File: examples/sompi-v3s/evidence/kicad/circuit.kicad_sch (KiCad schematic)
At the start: 132 parts, among them J1 USB-C 16P, J2 RJ45 HR911105A, J3 microSD, J4 LCD 40P RGB, J5 CAM MIPI 24P, J6 3.5mm jack, J7 GPIO 2x13, J8 UART0 debug, Q1 AO3400A, SW1 RESET, SW2 KEY1, U1 Allwinner V3s, U2 TPS562200, U3 TPS562200, U4 ME6211C18M5G, U5 XC6206P302MR, U6 W25Q128JVSIQ, U8 USBLC6-2SC6, Y1 24MHz, Y2 32.768kHz

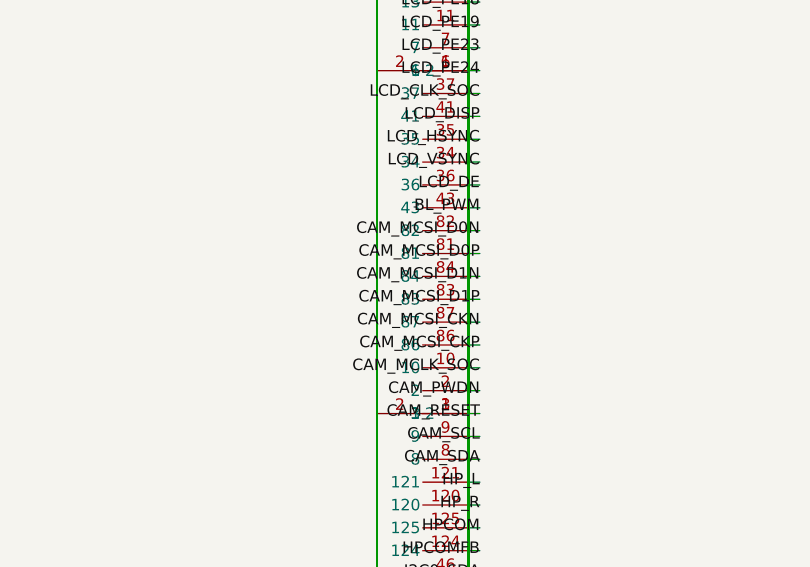
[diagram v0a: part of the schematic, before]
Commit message: evidence: SomPi-V3s rebuilt with someda 0.7.0 — 7 of 7 pairs coupled within skew budget, 0 crosstalk violations, kicad-cli DRC 0 errors, 6/6 gates
Co-Authored-By: Claude Fable 5.1 <noreply@anthropic.com>
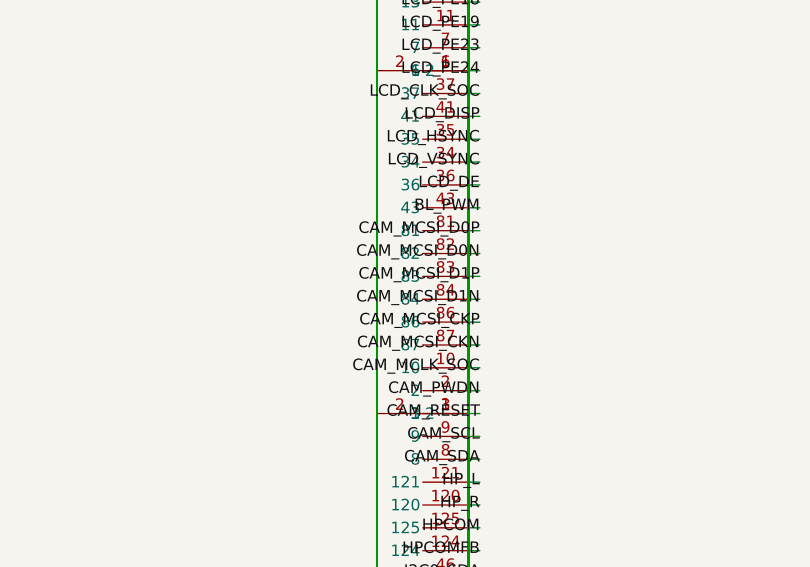
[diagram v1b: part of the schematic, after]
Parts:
- U1: symbol SoC:Allwinner_V3s__p129_12_29_50_57_104_127_85_93_98_109_122_19_58_64_80_108_126_20_21_25_26_38_47_51_56_88_59_60_61_62_65_66_67_68_69_70_72_79_76_115_97_116_123_71_63_73_117_118_94_75_74_96_95_99_112_42_111_110_92_91_90_89_77_78_101_102_103_106_107_105_100_54_52_55_53_33_32_31_30_28_27_24_23_22_18_17_16_15_14_13_11_7_6_37_41_35_34_36_43_82_81_84_83_87_86_10_2_3_9_8_121_120_125_124_46_45_5_39_40_4_44_1_128_48_49 -> SoC:Allwinner_V3s__p129_12_29_50_57_104_127_85_93_98_109_122_19_58_64_80_108_126_20_21_25_26_38_47_51_56_88_59_60_61_62_65_66_67_68_69_70_72_79_76_115_97_116_123_71_63_73_117_118_94_75_74_96_95_99_112_42_111_110_92_91_90_89_77_78_101_102_103_106_107_105_100_54_52_55_53_33_32_31_30_28_27_24_23_22_18_17_16_15_14_13_11_7_6_37_41_35_34_36_43_81_82_83_84_86_87_10_2_3_9_8_121_120_125_124_46_45_5_39_40_4_44_1_128_48_49
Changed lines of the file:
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@@
   (wire (pts (xy 45.72 2141.22) (xy 45.72 2222.50)) (uuid wire_1144) )
   (wire (pts (xy 55.88 144.78) (xy 57.15 144.78)) (uuid wire_1145) )
-  (label "CAM_MCSI_D0N" (at 57.15 144.78 180))
+  (label "CAM_MCSI_D0P" (at 57.15 144.78 180))
   (wire (pts (xy 55.88 147.32) (xy 55.88 2136.14)) (uuid wire_1146) )
   (wire (pts (xy 55.88 2136.14) (xy 55.88 2136.14)) (uuid wire_1147) )
   (wire (pts (xy 55.88 2136.14) (xy 55.88 2222.50)) (uuid wire_1148) )
   (wire (pts (xy 55.88 147.32) (xy 57.15 147.32)) (uuid wire_1149) )
-  (label "CAM_MCSI_D0P" (at 57.15 147.32 180))
+  (label "CAM_MCSI_D0N" (at 57.15 147.32 180))
   (wire (pts (xy 55.88 149.86) (xy 55.88 2131.06)) (uuid wire_1150) )
   (wire (pts (xy 55.88 2131.06) (xy 55.88 2131.06)) (uuid wire_1151) )
   (wire (pts (xy 55.88 2131.06) (xy 55.88 2225.04)) (uuid wire_1152) )
   (wire (pts (xy 55.88 149.86) (xy 57.15 149.86)) (uuid wire_1153) )
-  (label "CAM_MCSI_D1N" (at 57.15 149.86 180))
+  (label "CAM_MCSI_D1P" (at 57.15 149.86 180))
   (wire (pts (xy 55.88 152.40) (xy 55.88 2125.98)) (uuid wire_1154) )
   (wire (pts (xy 55.88 2125.98) (xy 55.88 2125.98)) (uuid wire_1155) )
   (wire (pts (xy 55.88 2125.98) (xy 55.88 2227.58)) (uuid wire_1156) )
   (wire (pts (xy 55.88 152.40) (xy 57.15 152.40)) (uuid wire_1157) )
-  (label "CAM_MCSI_D1P" (at 57.15 152.40 180))
+  (label "CAM_MCSI_D1N" (at 57.15 152.40 180))
   (wire (pts (xy 55.88 154.94) (xy 55.88 2120.90)) (uuid wire_1158) )
   (wire (pts (xy 55.88 2120.90) (xy 55.88 2120.90)) (uuid wire_1159) )
   (wire (pts (xy 55.88 2120.90) (xy 55.88 2230.12)) (uuid wire_1160) )
   (wire (pts (xy 55.88 154.94) (xy 57.15 154.94)) (uuid wire_1161) )
-  (label "CAM_MCSI_CKN" (at 57.15 154.94 180))
+  (label "CAM_MCSI_CKP" (at 57.15 154.94 180))
   (wire (pts (xy 55.88 157.48) (xy 55.88 2115.82)) (uuid wire_1162) )
   (wire (pts (xy 55.88 2115.82) (xy 55.88 2115.82)) (uuid wire_1163) )
   (wire (pts (xy 55.88 2115.82) (xy 55.88 2232.66)) (uuid wire_1164) )
   (wire (pts (xy 55.88 157.48) (xy 57.15 157.48)) (uuid wire_1165) )
-  (label "CAM_MCSI_CKP" (at 57.15 157.48 180))
+  (label "CAM_MCSI_CKN" (at 57.15 157.48 180))
   (wire (pts (xy 55.88 160.02) (xy 55.88 2110.74)) (uuid wire_1166) )
   (wire (pts (xy 55.88 2110.74) (xy 109.22 2110.74)) (uuid wire_1167) )
@@
   (wire (pts (xy 55.88 208.28) (xy 57.15 208.28)) (uuid wire_1271) )
   (label "UART0_RX" (at 57.15 208.28 180))
-  (symbol (lib_id "SoC:Allwinner_V3s__p129_12_29_50_57_104_127_85_93_98_109_122_19_58_64_80_108_126_20_21_25_26_38_47_51_56_88_59_60_61_62_65_66_67_68_69_70_72_79_76_115_97_116_123_71_63_73_117_118_94_75_74_96_95_99_112_42_111_110_92_91_90_89_77_78_101_102_103_106_107_105_100_54_52_55_53_33_32_31_30_28_27_24_23_22_18_17_16_15_14_13_11_7_6_37_41_35_34_36_43_82_81_84_83_87_86_10_2_3_9_8_121_120_125_124_46_45_5_39_40_4_44_1_128_48_49") (at 50.80 50.80 0) (unit 1)
+  (symbol (lib_id "SoC:Allwinner_V3s__p129_12_29_50_57_104_127_85_93_98_109_122_19_58_64_80_108_126_20_21_25_26_38_47_51_56_88_59_60_61_62_65_66_67_68_69_70_72_79_76_115_97_116_123_71_63_73_117_118_94_75_74_96_95_99_112_42_111_110_92_91_90_89_77_78_101_102_103_106_107_105_100_54_52_55_53_33_32_31_30_28_27_24_23_22_18_17_16_15_14_13_11_7_6_37_41_35_34_36_43_81_82_83_84_86_87_10_2_3_9_8_121_120_125_124_46_45_5_39_40_4_44_1_128_48_49") (at 50.80 50.80 0) (unit 1)
 (property "Reference" "U1" (at 0 -5 0))
 (property "Value" "Allwinner V3s" (at 0 5 0))

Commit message: feat: fetch-libs step, repair-loop and connector-orientation contract, SomPi evidence rebuilt (someda 1d11b951fee7)
- scripts/fetch-libs.py + setup_libraries: KiCad GitLab, LCSC/EasyEDA by lcsc or mpn
  (JLCPCB parts search), vendor zip import; every part ends FOUND / FETCHED / MISSING
- SKILL.md, pcb-plan.md, pcb-build.md, CONTRACT.md: schematic approval -> fetch-libs ->
  build with the engine's repair rounds (SOMEDA_REPAIR_ROUNDS, repair:/suggest: lines,
  plan.built.json); edge_overhang_mm and engine-derived connector rotations; placement
  order and island growth documented
- examples/sompi-v3s: plan without connector rotations (the engine orients), pairs, part
  numbers; evidence of the final 0.7.0 build: 187/187 routed, 7/7 pairs within skew
  budget, 0 crosstalk violations, kicad-cli DRC 0 errors, all six gates, schematic
  PDF/SVG, 3D renders, detailed BOM, JLCPCB order package

Co-Authored-By: Claude Fable 5.1 <noreply@anthropic.com>
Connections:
- net +1V2: no longer C1.2, C10.1, C10.2, C11.1, C11.2, C12.1, C12.2, C13.1, C13.2, C14.1, C14.2, C15.1, C15.2, C16.1, C16.2, C17.1, C17.2, C18.1, C18.2, C19.1, C19.2, C2.2, C20.1, C20.2, C21.1, C21.2, C22.1, C22.2, C23.1, C23.2, C24.1, C24.2, C25.1, C25.2, C26.1, C26.2, C27.1, C27.2, C28.1, C28.2, C29.1, C29.2, C3.2, C30.1, C30.2, C31.1, C31.2, C32.1, C32.2, C33.1, C33.2, C34.1, C34.2, C35.1, C35.2, C36.1, C36.2, C37.1, C37.2, C38.1, C38.2, C39.1, C39.2, C4.2, C40.1, C40.2, C41.1, C41.2, C42.1, C42.2, C43.1, C43.2, C44.1, C44.2, C45.1, C45.2, C46.1, C46.2, C47.2, C48.2, C49.1, C49.2, C5.2, C50.1, C50.2, C51.1, C51.2, C52.1, C52.2, C53.1, C53.2, C54.1, C54.2, C55.1, C55.2, C56.1, C56.2, C57.1, C57.2, C58.1, C58.2, C59.1, C59.2, C6.2, C7.2, C8.2, C9.1, C9.2, D1.1, D1.2, D2.1, D2.2, F1.1, F1.2, J1.A1, J1.A12, J1.A4, J1.A5, J1.A6, J1.A7, J1.A9, J1.B1, J1.B12, J1.B4, J1.B5, J1.B6, J1.B7, J1.B9, J1.SH, J2.1, J2.10, J2.11, J2.12, J2.2, J2.3, J2.4, J2.5, J2.6, J2.8, J2.9, J2.SH, J3.1, J3.10, J3.2, J3.3, J3.4, J3.5, J3.6, J3.7, J3.8, J3.9, J3.SH, J4.1, J4.10, J4.11, J4.12, J4.15, J4.16, J4.17, J4.18, J4.19, J4.2, J4.20, J4.23, J4.24, J4.25, J4.26, J4.27, J4.28, J4.29, J4.3, J4.30, J4.31, J4.32, J4.33, J4.34, J4.36, J4.4, J4.7, J4.8, J4.9, J4.MP, J5.1, J5.10, J5.11, J5.12, J5.13, J5.14, J5.15, J5.16, J5.17, J5.18, J5.19, J5.2, J5.3, J5.4, J5.5, J5.6, J5.7, J5.8, J5.9, J5.MP, J6.R, J6.S, J6.T, J7.1, J7.10, J7.11, J7.12, J7.13, J7.14, J7.15, J7.17, J7.2, J7.20, J7.25, J7.3, J7.4, J7.5, J7.6, J7.7, J7.8, J7.9, J8.1, J8.2, J8.3, L1.1, L1.2, L2.1, L3.1, L3.2, Q1.1, Q1.2, Q1.3, R1.1, R1.2, R10.1, R10.2, R11.1, R11.2, R12.1, R12.2, R13.1, R13.2, R14.1, R14.2, R15.1, R15.2, R16.1, R16.2, R17.1, R17.2, R18.1, R18.2, R19.2, R2.1, R2.2, R20.1, R20.2, R21.1, R21.2, R22.1, R22.2, R23.1, R23.2, R24.1, R24.2, R25.1, R25.2, R26.1, R26.2, R27.1, R27.2, R28.1, R28.2, R29.1, R29.2, R3.1, R3.2, R30.1, R30.2, R31.1, R31.2, R32.1, R32.2, R33.1, R33.2, R34.1, R34.2, R35.1, R35.2, R36.1, R36.2, R37.1, R37.2, R38.1, R38.2, R39.1, R39.2, R4.1, R4.2, R40.1, R40.2, R41.1, R41.2, R42.1, R42.2, R43.1, R43.2, R5.1, R5.2, R6.1, R6.2, R7.1, R7.2, R8.1, R8.2, R9.1, R9.2, SW1.1, SW1.2, SW2.1, SW2.2, U1.1, U1.10, U1.100, U1.101, U1.102, U1.103, U1.104, U1.105, U1.106, U1.107, U1.109, U1.11, U1.110, U1.111, U1.112, U1.115, U1.116, U1.117, U1.118, U1.12, U1.120, U1.121, U1.122, U1.123, U1.124, U1.125, U1.127, U1.128, U1.129, U1.13, U1.14, U1.15, U1.16, U1.17, U1.18, U1.2, U1.22, U1.23, U1.24, U1.27, U1.28, U1.29, U1.3, U1.30, U1.31, U1.32, U1.33, U1.34, U1.35, U1.36, U1.37, U1.39, U1.4, U1.40, U1.41, U1.42, U1.43, U1.44, U1.45, U1.46, U1.48, U1.49, U1.5, U1.50, U1.52, U1.53, U1.54, U1.55, U1.57, U1.59, U1.6, U1.60, U1.61, U1.62, U1.63, U1.65, U1.66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
- new net +1V8: C10.1, C11.1, C12.1, C13.1, C14.1, C15.1, C50.1, C58.1, C9.1, J5.18, R1.1, R3.1, U1.59, U1.60, U1.61, U1.62, U1.65, U1.66, U1.67, U1.68, U1.69, U1.70, U1.72, U1.79, U4.5
- new net +3V0: C24.1, C25.1, C26.1, C52.1, R11.1, U1.115, U1.76, U5.2
- new net +3V3: C16.1, C17.1, C18.1, C19.1, C20.1, C21.1, C22.1, C23.1, C43.1, C44.1, C49.1, C51.1, C55.1, C56.1, C57.1, J3.4, J4.4, J5.16, J7.1, J7.17, L1.2, L3.1, R10.1, R13.1, R17.1, R25.1, R26.1, R27.1, R28.1, R29.1, R30.1, R31.1, R33.1, R38.1, R39.1, R42.1, R43.1, U1.104, U1.109, U1.12, U1.122, U1.127, U1.29, U1.50, U1.57, U1.85, U1.93, U1.98, U4.1, U4.3, U5.3, U6.3, U6.7, U6.8
- new net AGND: C24.2, C25.2, C26.2, C32.2, C33.2, R7.1, U1.116
- new net BL_GATE: Q1.1, R35.2, R36.1
- new net BL_PWM: R35.1, U1.43
- new net CAM_MCLK: J5.11, R37.2
- new net CAM_MCLK_SOC: R37.1, U1.10
- new net CAM_MCSI_CKN: J5.9, U1.87
- new net CAM_MCSI_CKP: J5.8, U1.86
- new net CAM_MCSI_D0N: J5.3, U1.82
- new net CAM_MCSI_D0P: J5.2, U1.81
- new net CAM_MCSI_D1N: J5.6, U1.84
- new net CAM_MCSI_D1P: J5.5, U1.83
- new net CAM_PWDN: J5.12, U1.2
- new net CAM_RESET: J5.13, U1.3
- new net CAM_SCL: J5.14, R38.2, U1.9
- new net CAM_SDA: J5.15, R39.2, U1.8
- new net CC1: J1.A5, R15.1
- new net CC2: J1.B5, R16.1
- new net EPHY_RTX: R8.1, U1.94
- new net ETH_LED_A1: J2.9, R25.2
- new net ETH_LED_A2: J2.11, R26.2
- new net ETH_LED_LINK: J2.10, U1.77
- new net ETH_LED_SPD: J2.12, U1.78
- new net ETH_RXN: J2.6, R24.1, U1.89
- new net ETH_RXP: J2.3, R23.1, U1.90
- new net ETH_TXN: J2.2, R22.1, U1.91
- new net ETH_TXP: J2.1, R21.1, U1.92
- new net ETH_VCC: C53.1, C54.1, J2.4, J2.5, L3.2, R21.2, R22.2, R23.2, R24.2
- new net GND: C1.2, C10.2, C11.2, C12.2, C13.2, C14.2, C15.2, C16.2, C17.2, C18.2, C19.2, C2.2, C20.2, C21.2, C22.2, C23.2, C27.2, C28.2, C29.2, C3.2, C30.2, C31.2, C34.2, C35.2, C36.2, C37.2, C38.2, C39.2, C4.2, C40.2, C42.2, C43.2, C44.2, C46.2, C47.2, C48.2, C49.2, C5.2, C50.2, C51.2, C52.2, C53.2, C54.2, C55.2, C56.2, C57.2, C58.2, C59.2, C6.2, C7.2, C8.2, C9.2, D1.1, D2.1, J1.A1, J1.A12, J1.B1, J1.B12, J1.SH, J2.8, J2.SH, J3.10, J3.6, J3.SH, J4.29, J4.3, J4.36, J4.MP, J5.1, J5.10, J5.17, J5.19, J5.4, J5.7, J5.MP, J7.14, J7.20, J7.25, J7.6, J7.9, J8.1, Q1.2, R15.2, R16.2, R18.2, R2.2, R20.2, R36.2, R4.2, R5.2, R7.2, R8.2, SW1.2, SW2.2, U1.129, U2.1, U3.1, U4.2, U5.1, U6.4, U8.2, Y1.2, Y1.4
- new net GPIO_PG0: J7.7, U1.5
- new net GPIO_PG1: J7.11, U1.4
- new net GPIO_PG4: J7.13, U1.1
- new net GPIO_PG5: J7.15, U1.128
- new net HPCOM: R40.1, U1.125
- new net HPCOMFB: R41.1, U1.124
- new net HPCOM_OUT: C59.1, J6.S, R40.2, R41.2
- new net HPVCC_BP: C28.1, C29.1, U1.123
- new net HP_L: J6.T, U1.121
- new net HP_R: J6.R, U1.120
- new net I2C0_SCL: J7.5, R43.2, U1.45
- new net I2C0_SDA: J7.3, R42.2, U1.46
- new net KEY1: R12.2, SW2.1
- new net LCD_CLK: J4.30, R34.2
- new net LCD_CLK_SOC: R34.1, U1.37
- new net LCD_DE: J4.34, U1.36
- new net LCD_DISP: J4.31, U1.41
- new net LCD_HSYNC: J4.32, U1.35
- new net LCD_LEDK: J4.1, Q1.3
- new net LCD_PE10: J4.15, U1.24
- new net LCD_PE11: J4.16, U1.23
- new net LCD_PE12: J4.17, U1.22
- new net LCD_PE13: J4.18, U1.18
- new net LCD_PE14: J4.19, U1.17
- new net LCD_PE15: J4.20, U1.16
- new net LCD_PE16: J4.23, U1.15
- new net LCD_PE17: J4.24, U1.14
- new net LCD_PE18: J4.25, U1.13
- new net LCD_PE19: J4.26, U1.11
- new net LCD_PE23: J4.27, U1.7
- new net LCD_PE24: J4.28, U1.6
- new net LCD_PE4: J4.7, U1.33
- new net LCD_PE5: J4.8, U1.32
- new net LCD_PE6: J4.9, U1.31
- new net LCD_PE7: J4.10, U1.30
- new net LCD_PE8: J4.11, U1.28
- new net LCD_PE9: J4.12, U1.27
- new net LCD_VSYNC: J4.33, U1.34
- new net LRADC0: C39.1, R11.2, R12.1, U1.112
- new net PB3_LED: R14.1, U1.42
- new net PWM1: J7.12, U1.44
- new net PWR_LED: D1.2, R13.2
- new net RESET_N: C38.1, R10.2, SW1.1, U1.99
- new net RTC_VIO: C27.1, U1.97
- new net SD_CD: J3.9, R33.2, U1.100
- new net SD_CLK: J3.5, R32.2
- new net SD_CLK_SOC: R32.1, U1.105
- new net SD_CMD: J3.3, R29.2, U1.103
- new net SD_D0: J3.7, R30.2, U1.106
- new net SD_D1: J3.8, R31.2, U1.107
- new net SD_D2: J3.1, R27.2, U1.101
- new net SD_D3: J3.2, R28.2, U1.102
- new net SPI0_CLK: U1.53, U6.6
- new net SPI0_CS: U1.54, U6.1
- new net SPI0_MISO: U1.52, U6.2
- new net SPI0_MOSI: U1.55, U6.5
- new net STAT_LED: D2.2, R14.2
- new net SVREF0: C30.1, R1.2, R2.1, U1.71
- new net SVREF1: C31.1, R3.2, R4.1, U1.63
- new net SZQ: R5.1, U1.73
- new net U2_BST: C41.1, U2.6
- new net U2_FB: R17.2, R18.1, U2.4
- new net U2_SW: C41.2, L1.1, U2.2
- new net U3_BST: C45.1, U3.6
- new net U3_FB: R19.2, R20.1, U3.4
- new net U3_SW: C45.2, L2.1, U3.2
- new net UART0_RX: J8.3, U1.49
- new net UART0_TX: J8.2, U1.48
- new net UART2_RX: J7.10, U1.40
- new net UART2_TX: J7.8, U1.39
- new net USB_DM: U1.110, U8.4
- new net USB_DM_J: J1.A7, J1.B7, U8.3
- new net USB_DP: U1.111, U8.6
- new net USB_DP_J: J1.A6, J1.B6, U8.1
- new net VBUS: C40.1, C42.1, C46.1, F1.2, J4.2, J7.2, J7.4, U2.3, U2.5, U3.3, U3.5, U8.5
- new net VBUS_IN: F1.1, J1.A4, J1.A9, J1.B4, J1.B9
- new net VRA1: C32.1, R6.2, U1.117
- new net VRA2: C33.1, R6.1, U1.118
- new net X24M_IN: C34.1, U1.75, Y1.1
- new net X24M_OUT: C35.1, U1.74, Y1.3
- new net X32K_IN: C36.1, R9.1, U1.96, Y2.1
- new net X32K_OUT: C37.1, R9.2, U1.95, Y2.2
